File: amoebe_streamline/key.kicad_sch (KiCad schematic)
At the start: 0 parts

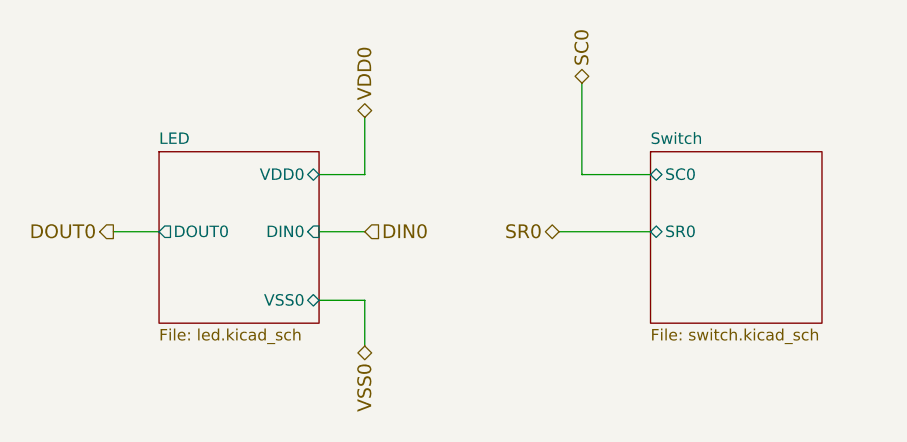
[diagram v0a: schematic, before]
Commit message: Finished schematic and routed traces
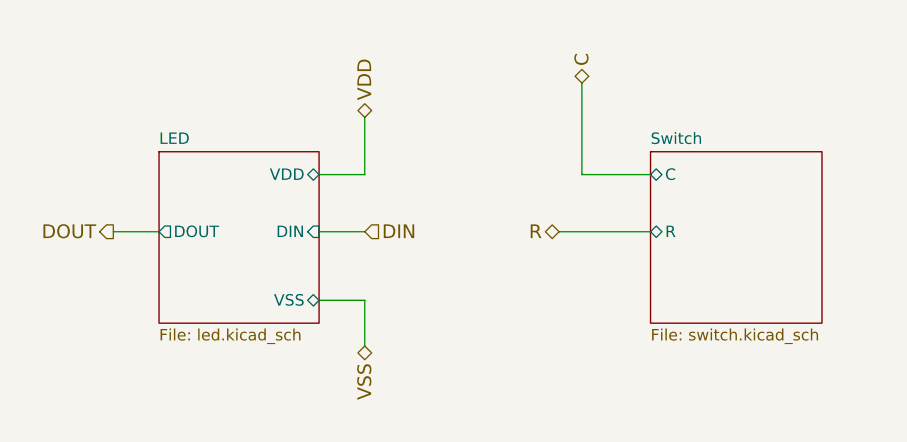
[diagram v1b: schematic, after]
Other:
- sheet LED ports: added DIN, DOUT, VDD, VSS; removed DIN0, DOUT0, VDD0, VSS0
- sheet Switch ports: added C, R; removed SC0, SR0
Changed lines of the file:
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@@
     (stroke (width 0) (type default))
   )
-  (hierarchical_label "DOUT0" (shape output) (at 102.87 93.98 180) (fields_autoplaced)
+  (hierarchical_label "DOUT" (shape output) (at 102.87 93.98 180) (fields_autoplaced)
     (effects (font (size 1.524 1.524)) (justify right))
   )
-  (hierarchical_label "SC0" (shape bidirectional) (at 154.94 77.47 90) (fields_autoplaced)
+  (hierarchical_label "C" (shape bidirectional) (at 154.94 77.47 90) (fields_autoplaced)
     (effects (font (size 1.524 1.524)) (justify left))
   )
-  (hierarchical_label "DIN0" (shape input) (at 130.81 93.98 0) (fields_autoplaced)
+  (hierarchical_label "DIN" (shape input) (at 130.81 93.98 0) (fields_autoplaced)
     (effects (font (size 1.524 1.524)) (justify left))
   )
-  (hierarchical_label "VDD0" (shape bidirectional) (at 130.81 81.28 90) (fields_autoplaced)
+  (hierarchical_label "VDD" (shape bidirectional) (at 130.81 81.28 90) (fields_autoplaced)
     (effects (font (size 1.524 1.524)) (justify left))
   )
-  (hierarchical_label "VSS0" (shape bidirectional) (at 130.81 106.68 270) (fields_autoplaced)
+  (hierarchical_label "VSS" (shape bidirectional) (at 130.81 106.68 270) (fields_autoplaced)
     (effects (font (size 1.524 1.524)) (justify right))
   )
-  (hierarchical_label "SR0" (shape bidirectional) (at 152.4 93.98 180) (fields_autoplaced)
+  (hierarchical_label "R" (shape bidirectional) (at 152.4 93.98 180) (fields_autoplaced)
     (effects (font (size 1.524 1.524)) (justify right))
   )
@@
       (effects (font (size 1.27 1.27)) (justify left top))
     )
-    (pin "SC0" bidirectional (at 162.56 87.63 180)
+    (pin "C" bidirectional (at 162.56 87.63 180)
       (effects (font (size 1.27 1.27)) (justify left))
     )
-    (pin "SR0" bidirectional (at 162.56 93.98 180)
+    (pin "R" bidirectional (at 162.56 93.98 180)
       (effects (font (size 1.27 1.27)) (justify left))
     )
@@
       (effects (font (size 1.27 1.27)) (justify left top))
     )
-    (pin "VSS0" bidirectional (at 125.73 101.6 0)
+    (pin "VSS" bidirectional (at 125.73 101.6 0)
       (effects (font (size 1.27 1.27)) (justify right))
     )
-    (pin "DOUT0" output (at 107.95 93.98 180)
+    (pin "DOUT" output (at 107.95 93.98 180)
       (effects (font (size 1.27 1.27)) (justify left))
     )
-    (pin "DIN0" input (at 125.73 93.98 0)
+    (pin "DIN" input (at 125.73 93.98 0)
       (effects (font (size 1.27 1.27)) (justify right))
     )
-    (pin "VDD0" bidirectional (at 125.73 87.63 0)
+    (pin "VDD" bidirectional (at 125.73 87.63 0)
       (effects (font (size 1.27 1.27)) (justify right))
     )
